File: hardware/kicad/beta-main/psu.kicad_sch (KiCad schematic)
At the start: 0 parts

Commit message: tweaks and added servo controller
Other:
- added sheet 12V (psu_12v.kicad_sch)
- added sheet Battery (psu_battery.kicad_sch)
- sheet 3V3 ports: added VIN; removed none
- sheet 5V ports: added VIN; removed none

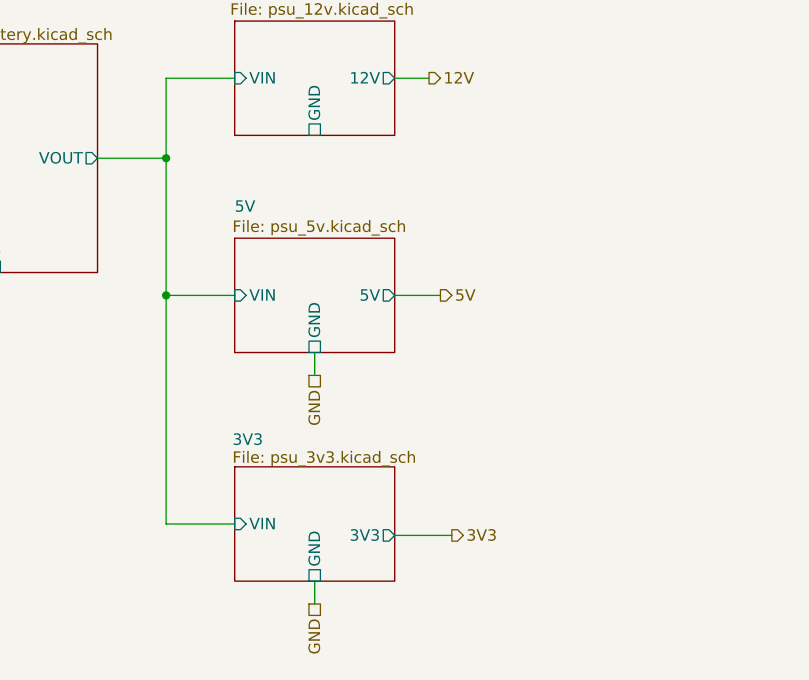
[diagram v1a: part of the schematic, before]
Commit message: add 5v power supply
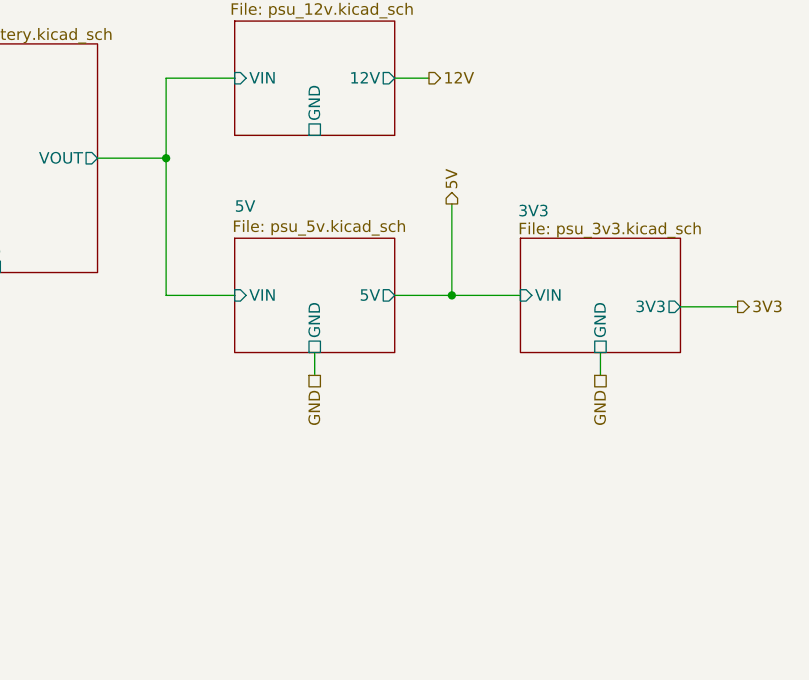
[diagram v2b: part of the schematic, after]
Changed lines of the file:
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@@
 	)
 	(junction
-		(at 52.07 66.04)
+		(at 83.82 66.04)
 		(diameter 0)
 		(color 0 0 0 0)
@@
 	(wire
 		(pts
-			(xy 77.47 92.71) (xy 83.82 92.71)
-		)
-		(stroke
-			(width 0)
-			(type default)
-		)
-	)
-	(wire
-		(pts
-			(xy 77.47 66.04) (xy 82.55 66.04)
-		)
-		(stroke
-			(width 0)
-			(type default)
-		)
-	)
-	(wire
-		(pts
-			(xy 52.07 91.44) (xy 59.69 91.44)
-		)
-		(stroke
-			(width 0)
-			(type default)
-		)
-	)
-	(wire
-		(pts
-			(xy 68.58 97.79) (xy 68.58 100.33)
+			(xy 109.22 67.31) (xy 115.57 67.31)
+		)
+		(stroke
+			(width 0)
+			(type default)
+		)
+	)
+	(wire
+		(pts
+			(xy 100.33 72.39) (xy 100.33 74.93)
 		)
 		(stroke
@@
 	(wire
 		(pts
-			(xy 52.07 91.44) (xy 52.07 66.04)
+			(xy 83.82 66.04) (xy 91.44 66.04)
 		)
 		(stroke
@@
 		(pts
 			(xy 52.07 41.91) (xy 59.69 41.91)
+		)
+		(stroke
+			(width 0)
+			(type default)
+		)
+	)
+	(wire
+		(pts
+			(xy 83.82 66.04) (xy 77.47 66.04)
+		)
+		(stroke
+			(width 0)
+			(type default)
+		)
+	)
+	(wire
+		(pts
+			(xy 83.82 55.88) (xy 83.82 66.04)
 		)
 		(stroke
@@
 	(hierarchical_label "GND"
 		(shape passive)
-		(at 68.58 100.33 270)
+		(at 100.33 74.93 270)
 		(effects
 			(font
@@
 	(hierarchical_label "5V"
 		(shape output)
-		(at 82.55 66.04 0)
+		(at 83.82 55.88 90)
 		(effects
 			(font
@@
 	(hierarchical_label "3V3"
 		(shape output)
-		(at 83.82 92.71 0)
+		(at 115.57 67.31 0)
 		(effects
 			(font
@@
 	)
 	(sheet
-		(at 59.69 85.09)
+		(at 91.44 59.69)
 		(size 17.78 12.7)
 		(exclude_from_sim no)
@@
 		)
 		(property "Sheetname" "3V3"
-			(at 59.436 82.804 0)
+			(at 91.186 57.404 0)
 			(effects
 				(font
@@
 		)
 		(property "Sheetfile" "psu_3v3.kicad_sch"
-			(at 59.436 83.312 0)
+			(at 91.186 57.912 0)
 			(effects
 				(font
@@
 		)
 		(pin "3V3" output
-			(at 77.47 92.71 0)
+			(at 109.22 67.31 0)
 			(effects
 				(font
@@
 		)
 		(pin "GND" passive
-			(at 68.58 97.79 270)
+			(at 100.33 72.39 270)
 			(effects
 				(font
@@
 		)
 		(pin "VIN" input
-			(at 59.69 91.44 180)
-			(effects
-				(font
+			(at 91.44 66.04 180)
+			(effects
+				(font

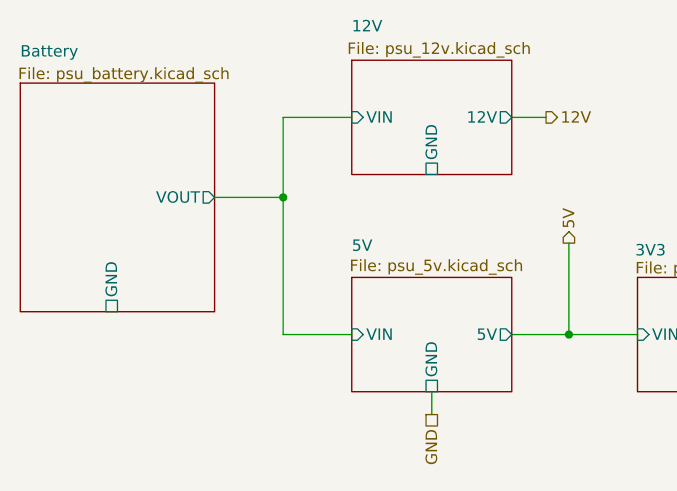
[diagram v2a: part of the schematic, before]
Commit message: 5V and amplifier corrections
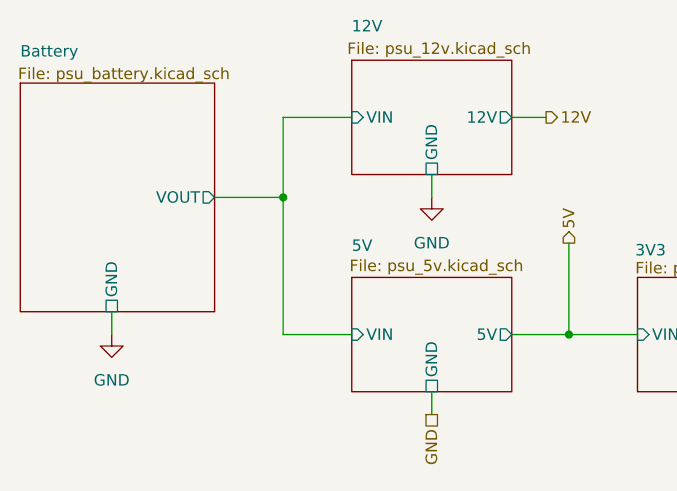
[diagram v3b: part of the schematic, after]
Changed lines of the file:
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@@
+	(wire
+		(pts
+			(xy 68.58 48.26) (xy 68.58 50.8)
+		)
+		(stroke
+			(width 0)
+			(type default)
+		)
+	)
 	(wire
 		(pts
 			(xy 100.33 72.39) (xy 100.33 74.93)
+		)
+		(stroke
+			(width 0)
+			(type default)
+		)
+	)
+	(wire
+		(pts
+			(xy 33.02 63.5) (xy 33.02 66.04)
 		)
 		(stroke
@@
 		)
 	)
+	(symbol
+		(lib_id "power:GND")
+		(at 68.58 50.8 0)
+		(unit 1)
+		(exclude_from_sim no)
+		(in_bom yes)
+		(on_board yes)
+		(dnp no)
+		(fields_autoplaced yes)
+		(property "Reference" "#PWR019"
+			(at 68.58 57.15 0)
+			(effects
+				(font
+					(size 1.27 1.27)
+				)
+				(hide yes)
+			)
+		)
+		(property "Value" "GND"
+			(at 68.58 55.88 0)
+			(effects
+				(font
+					(size 1.27 1.27)
+				)
+			)
+		)
+		(property "Footprint" ""
+			(at 68.58 50.8 0)
+			(effects
+				(font
+					(size 1.27 1.27)
+				)
+				(hide yes)
+			)
+		)
+		(property "Datasheet" ""
+			(at 68.58 50.8 0)
+			(effects
+				(font
+					(size 1.27 1.27)
+				)
+				(hide yes)
+			)
+		)
+		(property "Description" "Power symbol creates a global label with name \"GND\" , ground"
+			(at 68.58 50.8 0)
+			(effects
+				(font
+					(size 1.27 1.27)
+				)
+				(hide yes)
+			)
+		)
+		(pin "1"
+		)
+		(instances
+			(project "beta-main"
+				(path "/ec75fd42-4efa-4f32-b57e-76d632cb46f5/a42372fe-a5e6-45a2-9241-7a7c7af267fd"
+					(reference "#PWR019")
+					(unit 1)
+				)
+			)
+		)
+	)
+	(symbol
+		(lib_id "power:GND")
+		(at 33.02 66.04 0)
+		(unit 1)
+		(exclude_from_sim no)
+		(in_bom yes)
+		(on_board yes)
+		(dnp no)
+		(fields_autoplaced yes)
+		(property "Reference" "#PWR018"
+			(at 33.02 72.39 0)
+			(effects
+				(font
+					(size 1.27 1.27)
+				)
+				(hide yes)
+			)
+		)
+		(property "Value" "GND"
+			(at 33.02 71.12 0)
+			(effects
+				(font
+					(size 1.27 1.27)
+				)
+			)
+		)
+		(property "Footprint" ""
+			(at 33.02 66.04 0)
+			(effects
+				(font
+					(size 1.27 1.27)
+				)
+				(hide yes)
+			)
+		)
+		(property "Datasheet" ""
+			(at 33.02 66.04 0)
+			(effects
+				(font
+					(size 1.27 1.27)
+				)
+				(hide yes)
+			)
+		)
+		(property "Description" "Power symbol creates a global label with name \"GND\" , ground"
+			(at 33.02 66.04 0)
+			(effects
+				(font
+					(size 1.27 1.27)
+				)
+				(hide yes)
+			)
+		)
+		(pin "1"
+		)
+		(instances
+			(project "beta-main"
+				(path "/ec75fd42-4efa-4f32-b57e-76d632cb46f5/a42372fe-a5e6-45a2-9241-7a7c7af267fd"
+					(reference "#PWR018")
+					(unit 1)
+				)
+			)
+		)
+	)

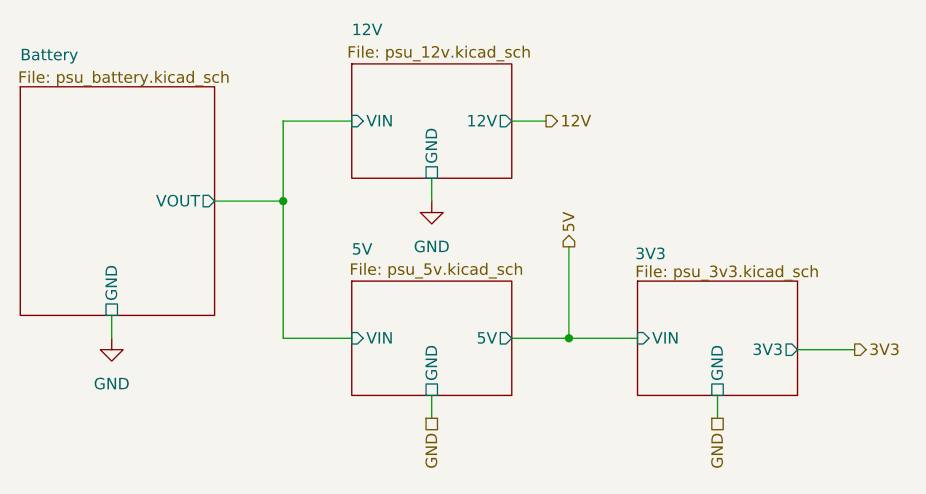
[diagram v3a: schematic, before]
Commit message: remove power symbols from hierarchy and move different subsystems  around
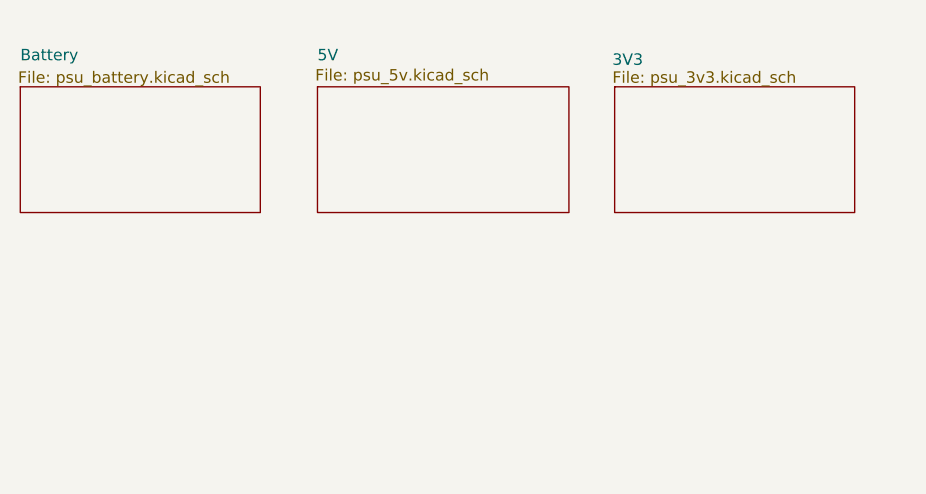
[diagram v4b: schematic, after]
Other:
- removed sheet 12V
- sheet 3V3 ports: added none; removed 3V3, GND, VIN
- sheet 5V ports: added none; removed 5V, GND, VIN
- sheet Battery ports: added none; removed GND, VOUT

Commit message: add modifications
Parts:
- added C10: 4.7nF, Capacitor_SMD:C_0402_1005Metric, symbol Device:C
- added C11, C14, C17, C19: 22u, Capacitor_SMD:C_0603_1608Metric_Pad1.08x0.95mm_HandSolder, symbol Device:C
- added C12: 100u, Capacitor_SMD:C_0603_1608Metric_Pad1.08x0.95mm_HandSolder, symbol Device:C_Polarized
- added C13, C15, C16, C18, C20, C3, C4, C5, C6, C9: 10u, Capacitor_SMD:C_0603_1608Metric_Pad1.08x0.95mm_HandSolder, symbol Device:C
- added C2: 220u, Capacitor_SMD:C_0603_1608Metric_Pad1.08x0.95mm_HandSolder, symbol Device:C_Polarized
- added C7, C8: 0.1u, Capacitor_SMD:C_0402_1005Metric, symbol Device:C
- added J18: XT60, Connector_AMASS:AMASS_XT60-F_1x02_P7.20mm_Vertical, symbol Connector:Conn_01x02_Socket
- added L1, L2: 2.2u, CM5IO:L_Bourns_SRP5030CC, symbol Device:L
- added R10: 10K 1%, Resistor_SMD:R_0402_1005Metric, symbol Device:R
- added R11: 2.2K 1%, Resistor_SMD:R_0402_1005Metric, symbol Device:R
- added R6: 100K 1%, Resistor_SMD:R_0402_1005Metric, symbol Device:R
- added R7: 220K, Resistor_SMD:R_0402_1005Metric, symbol Device:R
- added R8: 30K, Resistor_SMD:R_0402_1005Metric, symbol Device:R
- added R9: 15k, Resistor_SMD:R_0402_1005Metric, symbol Device:R
- added TP1: 5V, TestPoint:TestPoint_Pad_D1.0mm, symbol Connector:TestPoint
- added TP2: 3V3, TestPoint:TestPoint_Pad_D1.0mm, symbol Connector:TestPoint
- added U5: AP3441SHE-7B, Package_DFN_QFN:DFN-8-1EP_2x2mm_P0.5mm_EP1.05x1.75mm, symbol CM5IO:AP3441SHE-7B
- added U6: TPS56624x, Package_TO_SOT_SMD:SOT-563, symbol Beta:TPS56624x
- added U7: AP2553W6, Package_TO_SOT_SMD:SOT-23-6, symbol CM5IO:AP2553W6
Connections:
- new net: R7.2, R8.1, U6.6 (FB)
- new net: L1.1, U6.2 (SW)
- new net: R9.1, U7.5 (ILIM)
- new net: L2.1, U5.6 (LX)
- new net +3V3: C10.1, C13.1, C16.1, C18.1, C20.1, L2.2, R10.1, TP2.1
- new net +5V: C11.1, C14.1, C17.1, C19.1, C4.1, C5.1, C7.1, C9.1, L1.2, R6.1, R7.1, TP1.1, U5.3 (VIN), U5.7 (EN), U7.1 (IN)
- new net +BATT: C2.1, C3.1, C6.1, C8.1, J18.2 (Pin_2), U6.1 (VIN), U6.5 (EN)
- new net FB: C10.2, R10.2, R11.1, U5.1 (FB)
- new net GND: C11.2, C12.2, C13.2, C14.2, C15.2, C16.2, C17.2, C18.2, C19.2, C2.2, C20.2, C3.2, C4.2, C5.2, C6.2, C7.2, C8.2, C9.2, J18.1 (Pin_1), R11.2, R6.2, R8.2, R9.2, U5.4 (PGND), U5.8 (SGND), U5.9 (PAD), U6.3 (GND), U6.4 (AGND), U7.2 (GND)
- new net VBUS: C12.1, C15.1, U7.6 (OUT)
- new net VBUS_EN: U7.3 (EN)
- no-connect marks 0 -> 2
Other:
- removed sheet 3V3
- removed sheet 5V
- removed sheet Battery
- note added: "3.3V"
- note added: "5V"
- note added: "BATTERY PACK - POWER SOURCE"
- note added: "VBUS CURRENT LIMIT SWITCH"

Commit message: add filled zones and layout 5V and 3V3
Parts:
- C10, C7, C8: footprint Capacitor_SMD:C_0402_1005Metric -> Capacitor_SMD:C_0603_1608Metric
- C11, C13, C14, C15, C16, C17, C18, C19, C20, C3, C4, C5, C6, C9: footprint Capacitor_SMD:C_0603_1608Metric_Pad1.08x0.95mm_HandSolder -> Capacitor_SMD:C_0603_1608Metric
- C12, C2: footprint Capacitor_SMD:C_0603_1608Metric_Pad1.08x0.95mm_HandSolder -> (none)
- R10, R11, R6, R7, R8, R9: footprint Resistor_SMD:R_0402_1005Metric -> Resistor_SMD:R_0603_1608Metric

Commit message: add fan control
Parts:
- added C21: 10u, Capacitor_SMD:C_0603_1608Metric, symbol Device:C
- C12: footprint (none) -> Capacitor_SMD:CP_Elec_6.3x5.9
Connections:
- net GND: now also C21.2
- net VBUS: now also C21.1
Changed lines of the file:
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@@
 	(wire
 		(pts
+			(xy 228.6 139.7) (xy 218.44 139.7)
+		)
+		(stroke
+			(width 0)
+			(type default)
+		)
+	)
+	(wire
+		(pts
 			(xy 223.52 87.63) (xy 233.68 87.63)
 		)
@@
 	(wire
 		(pts
+			(xy 228.6 151.13) (xy 228.6 152.4)
+		)
+		(stroke
+			(width 0)
+			(type default)
+		)
+	)
+	(wire
+		(pts
 			(xy 119.38 49.53) (xy 119.38 53.34)
 		)
@@
 	(wire
 		(pts
+			(xy 228.6 143.51) (xy 228.6 139.7)
+		)
+		(stroke
+			(width 0)
+			(type default)
+		)
+	)
+	(wire
+		(pts
 			(xy 137.16 95.25) (xy 137.16 96.52)
 		)
@@
 			)
 		)
-		(property "Footprint" ""
+		(property "Footprint" "Capacitor_SMD:CP_Elec_6.3x5.9"
 			(at 207.9752 151.13 0)
 			(effects
@@
 	)
 	(symbol
+		(lib_id "Device:C")
+		(at 228.6 147.32 0)
+		(unit 1)
+		(exclude_from_sim no)
+		(in_bom yes)
+		(on_board yes)
+		(dnp no)
+		(property "Reference" "C21"
+			(at 231.521 146.1516 0)
+			(effects
+				(font
+					(size 1.27 1.27)
+				)
+				(justify left)
+			)
+		)
+		(property "Value" "10u"
+			(at 231.521 148.463 0)
+			(effects
+				(font
+					(size 1.27 1.27)
+				)
+				(justify left)
+			)
+		)
+		(property "Footprint" "Capacitor_SMD:C_0603_1608Metric"
+			(at 229.5652 151.13 0)
+			(effects
+				(font
+					(size 1.27 1.27)
+				)
+				(hide yes)
+			)
+		)
+		(property "Datasheet" "https://search.murata.co.jp/Ceramy/image/img/A01X/G101/ENG/GRM21BR71A106KA73-01.pdf"
+			(at 228.6 147.32 0)
+			(effects
+				(font
+					(size 1.27 1.27)
+				)
+				(hide yes)
+			)
+		)
+		(property "Description" ""
+			(at 228.6 147.32 0)
+			(effects
+				(font
+					(size 1.27 1.27)
+				)
+				(hide yes)
+			)
+		)
+		(property "Field4" "Digikey"
+			(at 228.6 147.32 0)
+			(effects
+				(font
+					(size 1.27 1.27)
+				)
+				(hide yes)
+			)
+		)
+		(property "Field5" "490-14381-1-ND"
+			(at 228.6 147.32 0)
+			(effects
+				(font
+					(size 1.27 1.27)
+				)
+				(hide yes)
+			)
+		)
+		(property "Field6" "GRM21BR71A106KA73L"
+			(at 228.6 147.32 0)
+			(effects
+				(font
+					(size 1.27 1.27)
+				)
+				(hide yes)
+			)
+		)
+		(property "Field7" "Murata"
+			(at 228.6 147.32 0)
+			(effects
+				(font
+					(size 1.27 1.27)
+				)
+				(hide yes)
+			)
+		)
+		(property "Field8" "111893011"
+			(at 228.6 147.32 0)
+			(effects
+				(font
+					(size 1.27 1.27)
+				)
+				(hide yes)
+			)
+		)
+		(property "Part Description" "	10uF 10% 10V Ceramic Capacitor X7R 0805 (2012 Metric)"
+			(at 228.6 147.32 0)
+			(effects
+				(font
+					(size 1.27 1.27)
+				)
+				(hide yes)
+			)
+		)
+		(property "Sim.Device" ""
+			(at 228.6 147.32 0)
+			(effects
+				(font
+					(size 1.27 1.27)
+				)
+				(hide yes)
+			)
+		)
+		(property "Sim.Pins" ""
+			(at 228.6 147.32 0)
+			(effects
+				(font
+					(size 1.27 1.27)
+				)
+				(hide yes)
+			)
+		)
+		(property "Sim.Type" ""
+			(at 228.6 147.32 0)
+			(effects
+				(font
+					(size 1.27 1.27)
+				)
+				(hide yes)
+			)
+		)
+		(pin "1"
+		)
+		(pin "2"
+		)
+		(instances
+			(project "beta-main"
+				(path "/6834c9e9-3e61-4f01-9d2c-ccd95d8f63cf/77db638e-233d-4258-91cb-4a238d3a7609"
+					(reference "C21")
+					(unit 1)
+				)
+			)
+		)
+	)
+	(symbol
 		(lib_id "power:GND")
 		(at 214.63 55.88 0)
@@
 					(unit 1)
 				)
+			)
+		)
+	)
+	(symbol
+		(lib_id "power:GND")
+		(at 228.6 152.4 0)
+		(unit 1)
+		(exclude_from_sim no)
+		(in_bom yes)
+		(on_board yes)
+		(dnp no)
+		(property "Reference" "#PWR0139"
+			(at 228.6 158.75 0)
+			(effects
+				(font
+					(size 1.27 1.27)
+				)
+				(hide yes)
+			)
+		)
+		(property "Value" "GND"
+			(at 228.727 156.7942 0)
+			(effects
+				(font
+					(size 1.27 1.27)
+				)
+			)
+		)
+		(property "Footprint" ""
+			(at 228.6 152.4 0)
+			(effects
+				(font
+					(size 1.27 1.27)
+				)
+				(hide yes)
+			)
+		)
+		(property "Datasheet" ""
+			(at 228.6 152.4 0)
+			(effects
+				(font
+					(size 1.27 1.27)
+				)
+				(hide yes)
+			)
+		)
+		(property "Description" "Power symbol creates a global label with name \"GND\" , ground"
+			(at 228.6 152.4 0)
+			(effects
+				(font
+					(size 1.27 1.27)
+				)
+				(hide yes)
+			)
+		)
+		(pin "1"
+		)
+		(instances
+			(project "beta-main"
+				(path "/6834c9e9-3e61-4f01-9d2c-ccd95d8f63cf/77db638e-233d-4258-91cb-4a238d3a7609"
+					(reference "#PWR0139")
+					(unit 1)
+				)
